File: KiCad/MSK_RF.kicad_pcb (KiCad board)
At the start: 2 copper layers, 52 x 73.5 mm, 65 parts, among them J1 Conn_01x05_Male, J2 Conn_01x12, J3 Conn_01x12, J4 Conn_Coaxial, J5 47346-0001, U1 STM32WLE5CCU6, U2 ADG918BRM, U3 TLV70233_SOT23-5, Y1 32.768 kHz, Y2 ECS-320-8-37-CKM-TR3

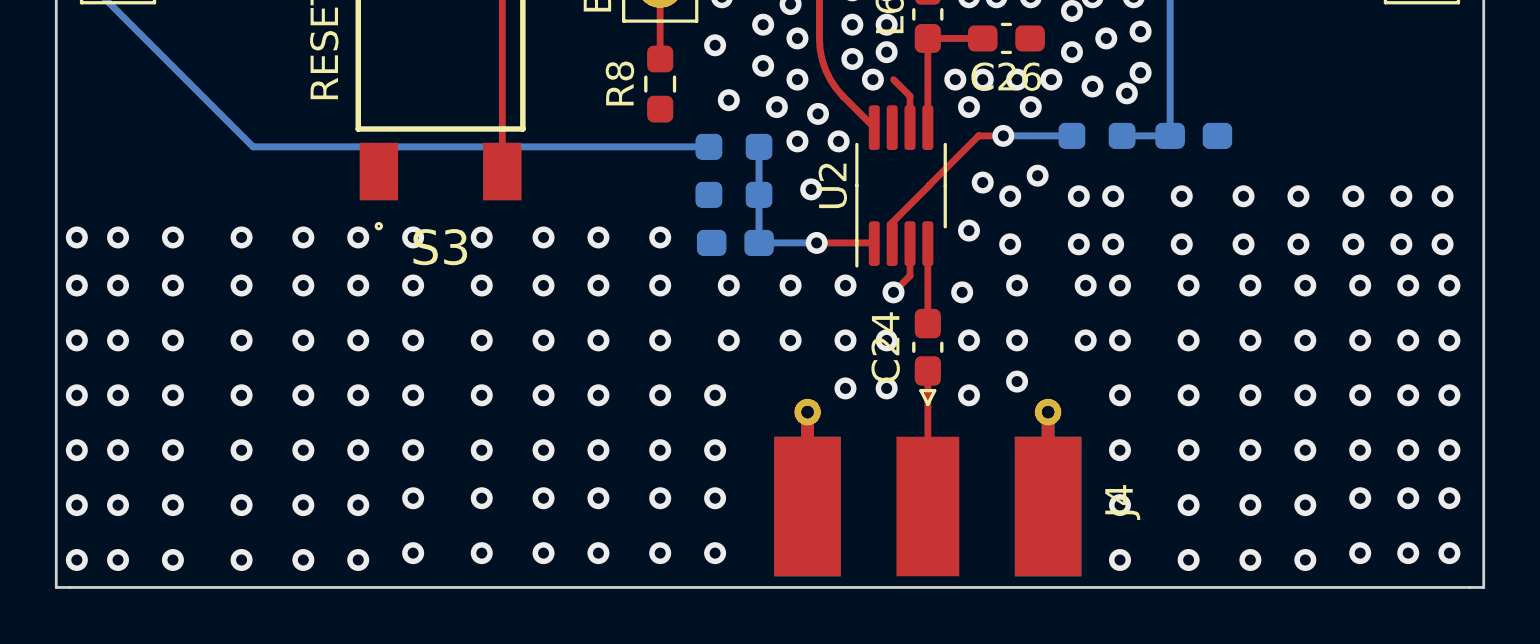
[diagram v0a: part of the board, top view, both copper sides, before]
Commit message: vias update
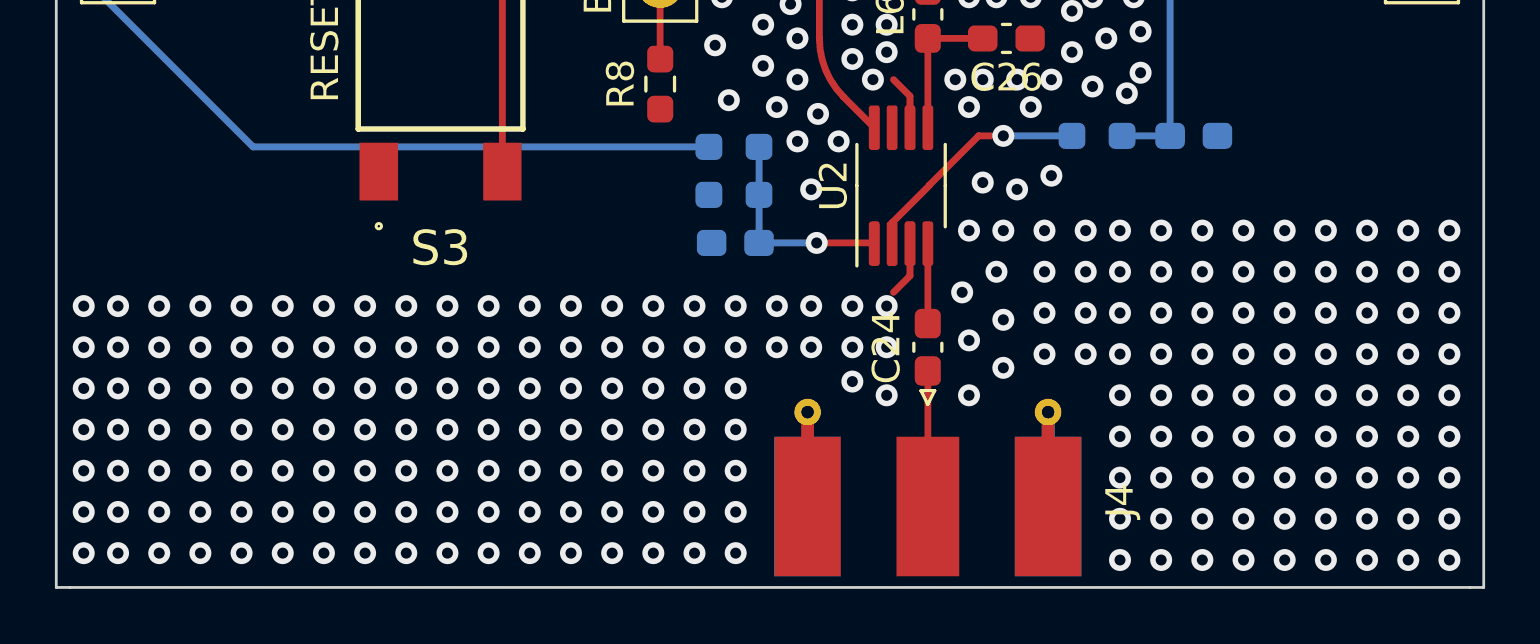
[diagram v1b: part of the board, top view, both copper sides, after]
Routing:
- net GND: vias 263 -> 330
